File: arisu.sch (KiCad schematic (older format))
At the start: 40 parts, among them J1 USB_B_Micro, J10 PF6, J11 PF7, J12 VCC, J13 D+, J14 D-, J15 GND, J2 MISO, J3 VCC, J4 SCK, J5 MOSI, J6 RES, J7 GND, J8 PF4, J9 PF5, U1 USBLC6-2SC6, U2 ATmega32U4-AU, Y1 Crystal_GND24

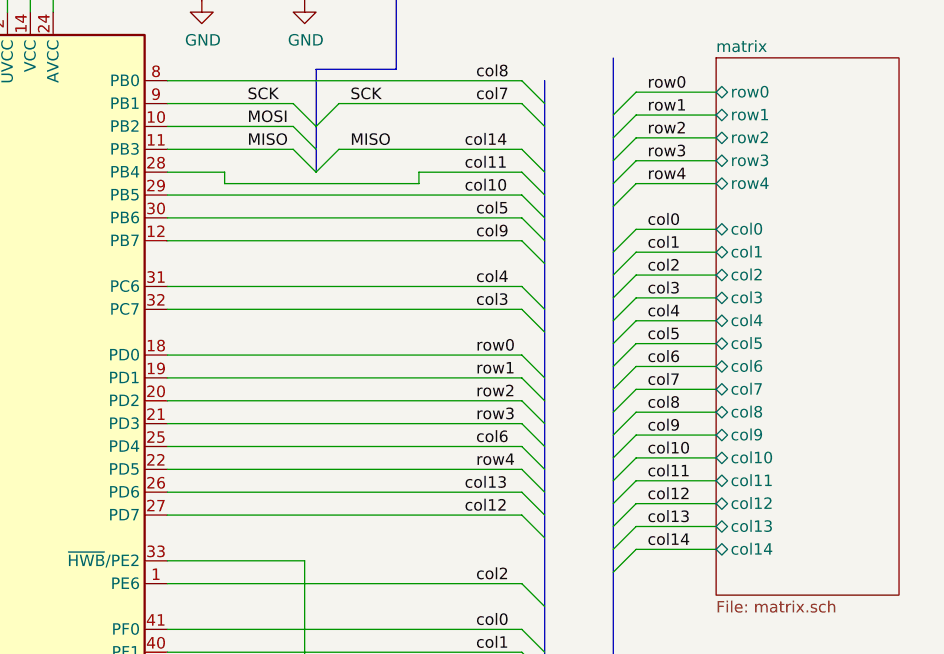
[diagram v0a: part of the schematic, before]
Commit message: Remove top row and decrease all other row indexes by 1 to adjust.
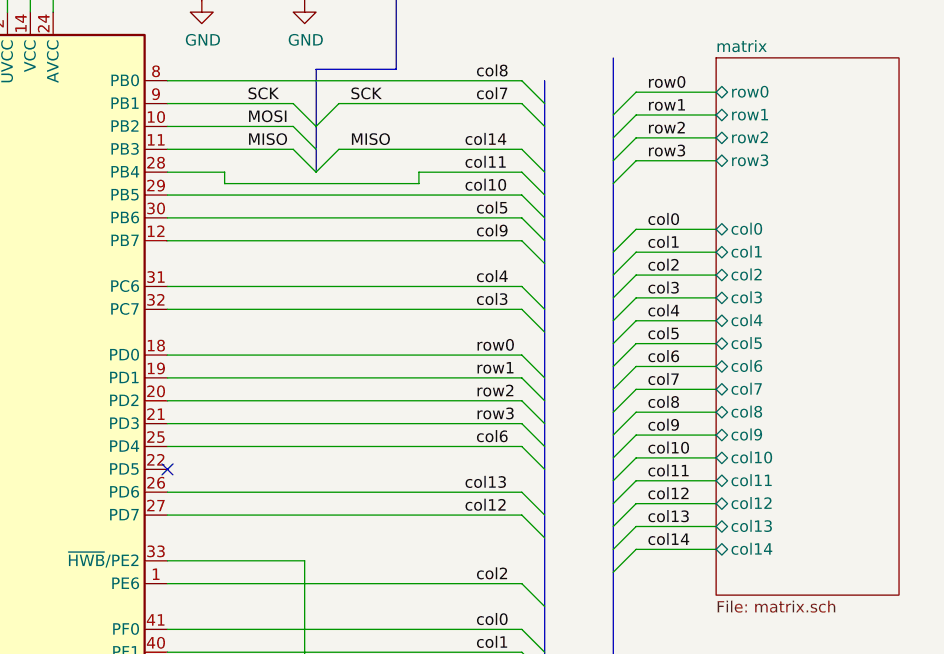
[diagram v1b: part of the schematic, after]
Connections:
- net row4: no longer names the net of U2.22 (PD5)
- no-connect marks 4 -> 5
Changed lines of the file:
@@
 EESchema Schematic File Version 4
 LIBS:arisu-cache
-EELAYER 26 0
+EELAYER 29 0
 EELAYER END
 $Descr A4 11693 8268
@@
 	5100 4350 6650 4350
 Wire Wire Line
-	5100 4450 6650 4450
-Wire Wire Line
 	5100 4550 6650 4550
 Wire Wire Line
@@
 Entry Wire Line
 	6650 4350 6750 4450
-Entry Wire Line
-	6650 4450 6750 4550
 Entry Wire Line
 	6650 4550 6750 4650
@@
 Text Label 6450 4250 0    50   ~ 0
 row3
-Text Label 6450 4450 0    50   ~ 0
-row4
 Text Label 6450 5150 0    50   ~ 0
 col0
@@
 F4 "row2" T L 7500 3000 50
 F5 "row3" T L 7500 3100 50
-F6 "row4" T L 7500 3200 50
-F7 "col0" T L 7500 3400 50
-F8 "col1" T L 7500 3500 50
-F9 "col2" T L 7500 3600 50
-F10 "col3" T L 7500 3700 50
-F11 "col4" T L 7500 3800 50
-F12 "col5" T L 7500 3900 50
-F13 "col6" T L 7500 4000 50
-F14 "col7" T L 7500 4100 50
-F15 "col8" T L 7500 4200 50
-F16 "col9" T L 7500 4300 50
-F17 "col10" T L 7500 4400 50
-F18 "col11" T L 7500 4500 50
-F19 "col12" T L 7500 4600 50
-F20 "col13" T L 7500 4700 50
-F21 "col14" T L 7500 4800 50
+F6 "col0" T L 7500 3400 50
+F7 "col1" T L 7500 3500 50
+F8 "col2" T L 7500 3600 50
+F9 "col3" T L 7500 3700 50
+F10 "col4" T L 7500 3800 50
+F11 "col5" T L 7500 3900 50
+F12 "col6" T L 7500 4000 50
+F13 "col7" T L 7500 4100 50
+F14 "col8" T L 7500 4200 50
+F15 "col9" T L 7500 4300 50
+F16 "col10" T L 7500 4400 50
+F17 "col11" T L 7500 4500 50
+F18 "col12" T L 7500 4600 50
+F19 "col13" T L 7500 4700 50
+F20 "col14" T L 7500 4800 50
 $EndSheet
 Wire Wire Line
@@
 Entry Wire Line
 	7050 3200 7150 3100
-Entry Wire Line
-	7050 3300 7150 3200
 Wire Wire Line
 	7150 3000 7500 3000
 Wire Wire Line
 	7150 3100 7500 3100
-Wire Wire Line
-	7150 3200 7500 3200
 Entry Wire Line
 	7050 3500 7150 3400
@@
 Wire Wire Line
 	5100 3150 5350 3150
-Text Label 7200 3200 0    50   ~ 0
-row4
 Text Label 7200 2800 0    50   ~ 0
 row0
@@
 	1    0    0    -1
 $EndComp
+$Comp
+L Mechanical:MountingHole H3
+U 1 1 5C59C18D
+P 8700 3100
+F 0 "H3" H 8800 3146 50  0000 L CNN
+F 1 "MountingHole" H 8800 3055 50  0000 L CNN
+F 2 "Mounting_Holes:MountingHole_2.2mm_M2_Pad" H 8700 3100 50  0001 C CNN
+F 3 "~" H 8700 3100 50  0001 C CNN
+	1    8700 3100
+	1    0    0    -1
+$EndComp
+$Comp
+L Mechanical:MountingHole H4
+U 1 1 5C59C1E9
+P 8700 3300
+F 0 "H4" H 8800 3346 50  0000 L CNN
+F 1 "MountingHole" H 8800 3255 50  0000 L CNN
+F 2 "Mounting_Holes:MountingHole_2.2mm_M2_Pad" H 8700 3300 50  0001 C CNN
+F 3 "~" H 8700 3300 50  0001 C CNN
+	1    8700 3300
+	1    0    0    -1
+$EndComp
+$Comp
+L Mechanical:MountingHole H5
+U 1 1 5C59C249
+P 8700 3500
+F 0 "H5" H 8800 3546 50  0000 L CNN
+F 1 "MountingHole" H 8800 3455 50  0000 L CNN
+F 2 "Mounting_Holes:MountingHole_2.2mm_M2_Pad" H 8700 3500 50  0001 C CNN
+F 3 "~" H 8700 3500 50  0001 C CNN
+	1    8700 3500
+	1    0    0    -1
+$EndComp
+$Comp
+L Mechanical:MountingHole H6
+U 1 1 5C59C2A7
+P 8700 3700
+F 0 "H6" H 8800 3746 50  0000 L CNN
+F 1 "MountingHole" H 8800 3655 50  0000 L CNN
+F 2 "Mounting_Holes:MountingHole_2.2mm_M2_Pad" H 8700 3700 50  0001 C CNN
+F 3 "~" H 8700 3700 50  0001 C CNN
+	1    8700 3700
+	1    0    0    -1
+$EndComp
+$Comp
+L Mechanical:MountingHole H7
+U 1 1 5C59C305
+P 8700 3900
+F 0 "H7" H 8800 3946 50  0000 L CNN
+F 1 "MountingHole" H 8800 3855 50  0000 L CNN
+F 2 "Mounting_Holes:MountingHole_2.2mm_M2_Pad" H 8700 3900 50  0001 C CNN
+F 3 "~" H 8700 3900 50  0001 C CNN
+	1    8700 3900
+	1    0    0    -1
+$EndComp
+$Comp
+L Mechanical:MountingHole H8
+U 1 1 5C59C367
+P 8700 4100
+F 0 "H8" H 8800 4146 50  0000 L CNN
+F 1 "MountingHole" H 8800 4055 50  0000 L CNN
+F 2 "Mounting_Holes:MountingHole_2.2mm_M2_Pad" H 8700 4100 50  0001 C CNN
+F 3 "~" H 8700 4100 50  0001 C CNN
+	1    8700 4100
+	1    0    0    -1
+$EndComp
+NoConn ~ 5100 4450
 Wire Bus Line
 	5750 2700 5750 3150
@@
 Wire Bus Line
 	7050 2650 7050 5800
-$Comp
-L Mechanical:MountingHole H3
-U 1 1 5C59C18D
-P 8700 3100
-F 0 "H3" H 8800 3146 50  0000 L CNN
-F 1 "MountingHole" H 8800 3055 50  0000 L CNN
-F 2 "Mounting_Holes:MountingHole_2.2mm_M2_Pad" H 8700 3100 50  0001 C CNN
-F 3 "~" H 8700 3100 50  0001 C CNN
-	1    8700 3100
-	1    0    0    -1
-$EndComp
-$Comp
-L Mechanical:MountingHole H4
-U 1 1 5C59C1E9
-P 8700 3300
-F 0 "H4" H 8800 3346 50  0000 L CNN
-F 1 "MountingHole" H 8800 3255 50  0000 L CNN
-F 2 "Mounting_Holes:MountingHole_2.2mm_M2_Pad" H 8700 3300 50  0001 C CNN
-F 3 "~" H 8700 3300 50  0001 C CNN
-	1    8700 3300
-	1    0    0    -1
-$EndComp
-$Comp
-L Mechanical:MountingHole H5
-U 1 1 5C59C249
-P 8700 3500
-F 0 "H5" H 8800 3546 50  0000 L CNN
-F 1 "MountingHole" H 8800 3455 50  0000 L CNN
-F 2 "Mounting_Holes:MountingHole_2.2mm_M2_Pad" H 8700 3500 50  0001 C CNN
-F 3 "~" H 8700 3500 50  0001 C CNN
-	1    8700 3500
-	1    0    0    -1
-$EndComp
-$Comp
-L Mechanical:MountingHole H6
-U 1 1 5C59C2A7
-P 8700 3700
-F 0 "H6" H 8800 3746 50  0000 L CNN
-F 1 "MountingHole" H 8800 3655 50  0000 L CNN
-F 2 "Mounting_Holes:MountingHole_2.2mm_M2_Pad" H 8700 3700 50  0001 C CNN
-F 3 "~" H 8700 3700 50  0001 C CNN
-	1    8700 3700
-	1    0    0    -1
-$EndComp
-$Comp
-L Mechanical:MountingHole H7
-U 1 1 5C59C305
-P 8700 3900
-F 0 "H7" H 8800 3946 50  0000 L CNN
-F 1 "MountingHole" H 8800 3855 50  0000 L CNN
-F 2 "Mounting_Holes:MountingHole_2.2mm_M2_Pad" H 8700 3900 50  0001 C CNN
-F 3 "~" H 8700 3900 50  0001 C CNN
-	1    8700 3900
-	1    0    0    -1
-$EndComp
-$Comp
-L Mechanical:MountingHole H8
-U 1 1 5C59C367
-P 8700 4100
-F 0 "H8" H 8800 4146 50  0000 L CNN
-F 1 "MountingHole" H 8800 4055 50  0000 L CNN
-F 2 "Mounting_Holes:MountingHole_2.2mm_M2_Pad" H 8700 4100 50  0001 C CNN
-F 3 "~" H 8700 4100 50  0001 C CNN
-	1    8700 4100
-	1    0    0    -1
-$EndComp
 $EndSCHEMATC

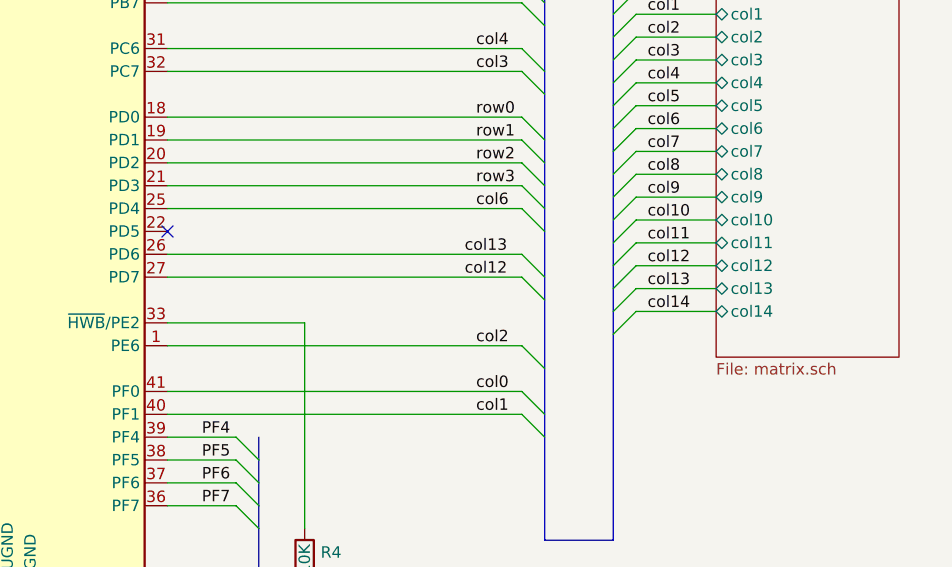
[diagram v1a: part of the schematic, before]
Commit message: Redesign alpha layout for natural finger spread.
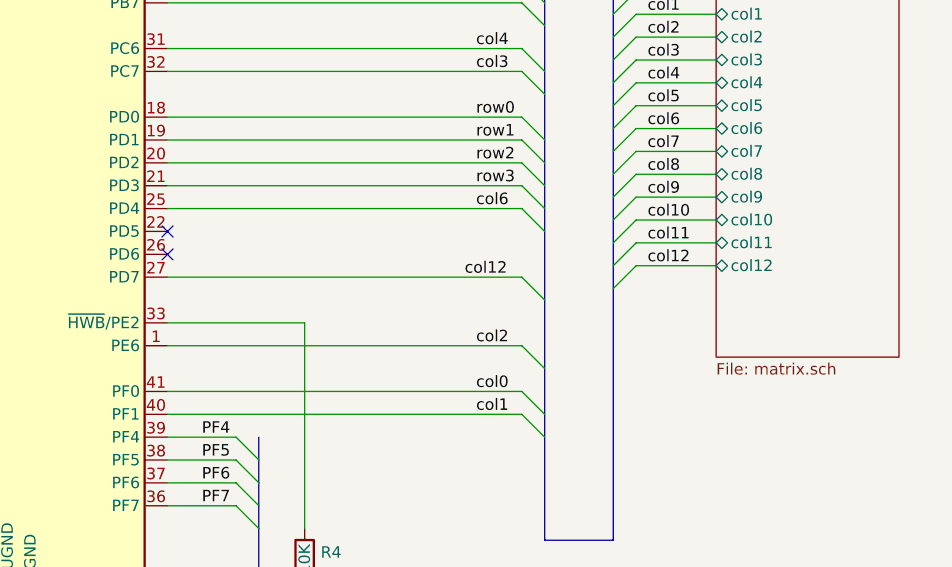
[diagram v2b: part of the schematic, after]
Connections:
- net col13: no longer names the net of U2.26 (PD6)
- no-connect marks 5 -> 6
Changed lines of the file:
@@
 	5100 4350 6650 4350
 Wire Wire Line
-	5100 4550 6650 4550
-Wire Wire Line
 	5100 4650 6650 4650
 Entry Wire Line
@@
 Entry Wire Line
 	6650 4350 6750 4450
-Entry Wire Line
-	6650 4550 6750 4650
 Entry Wire Line
 	6650 4650 6750 4750
@@
 Text Label 6400 4650 0    50   ~ 0
 col12
-Text Label 6400 4550 0    50   ~ 0
-col13
 Text Label 6400 3050 0    50   ~ 0
 col14
@@
 F17 "col11" T L 7500 4500 50
 F18 "col12" T L 7500 4600 50
-F19 "col13" T L 7500 4700 50
-F20 "col14" T L 7500 4800 50
 $EndSheet
 Wire Wire Line
@@
 Entry Wire Line
 	7050 4700 7150 4600
-Entry Wire Line
-	7050 4800 7150 4700
-Entry Wire Line
-	7050 4900 7150 4800
-Wire Wire Line
-	7150 4800 7500 4800
-Wire Wire Line
-	7150 4700 7500 4700
 Wire Wire Line
 	7150 4600 7500 4600
@@
 Text Label 7200 3500 0    50   ~ 0
 col1
-Text Label 7200 4800 0    50   ~ 0
-col14
-Text Label 7200 4700 0    50   ~ 0
-col13
 Text Label 7200 4600 0    50   ~ 0
 col12
@@
 $EndComp
 NoConn ~ 5100 4450
+NoConn ~ 5100 4550
 Wire Bus Line
 	5750 2700 5750 3150

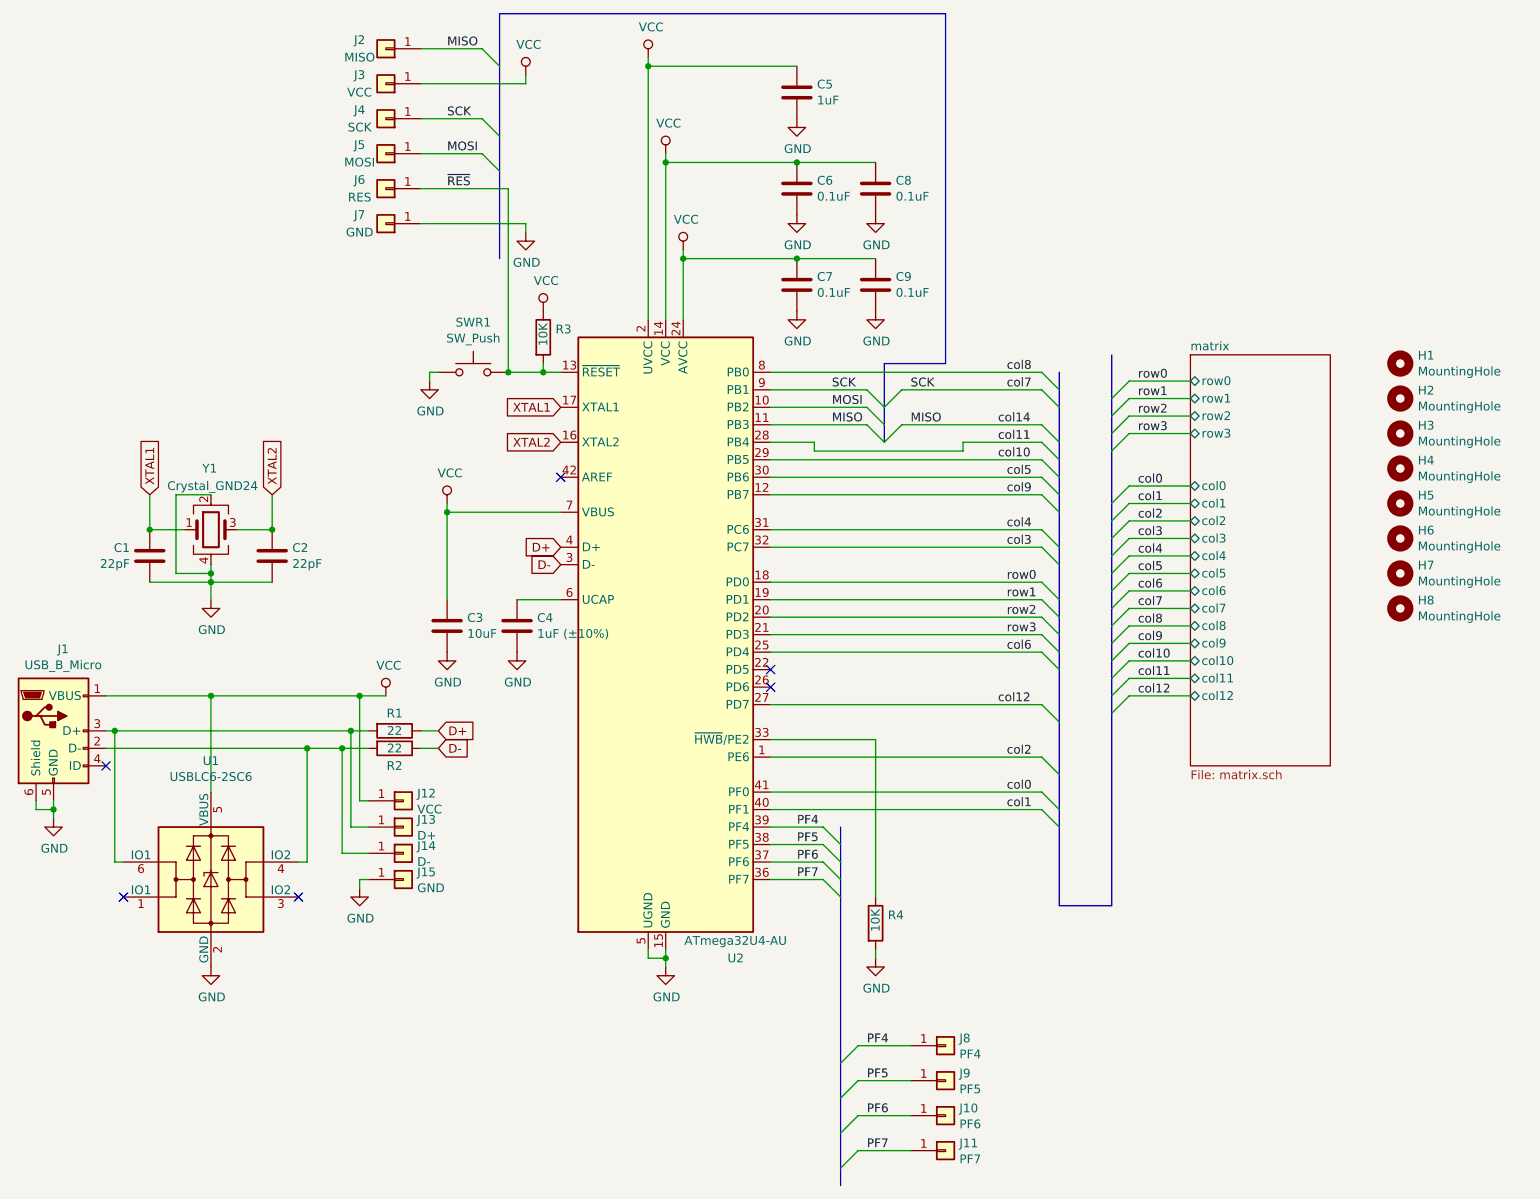
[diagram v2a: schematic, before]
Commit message: Finish ergo layout and route some rows.
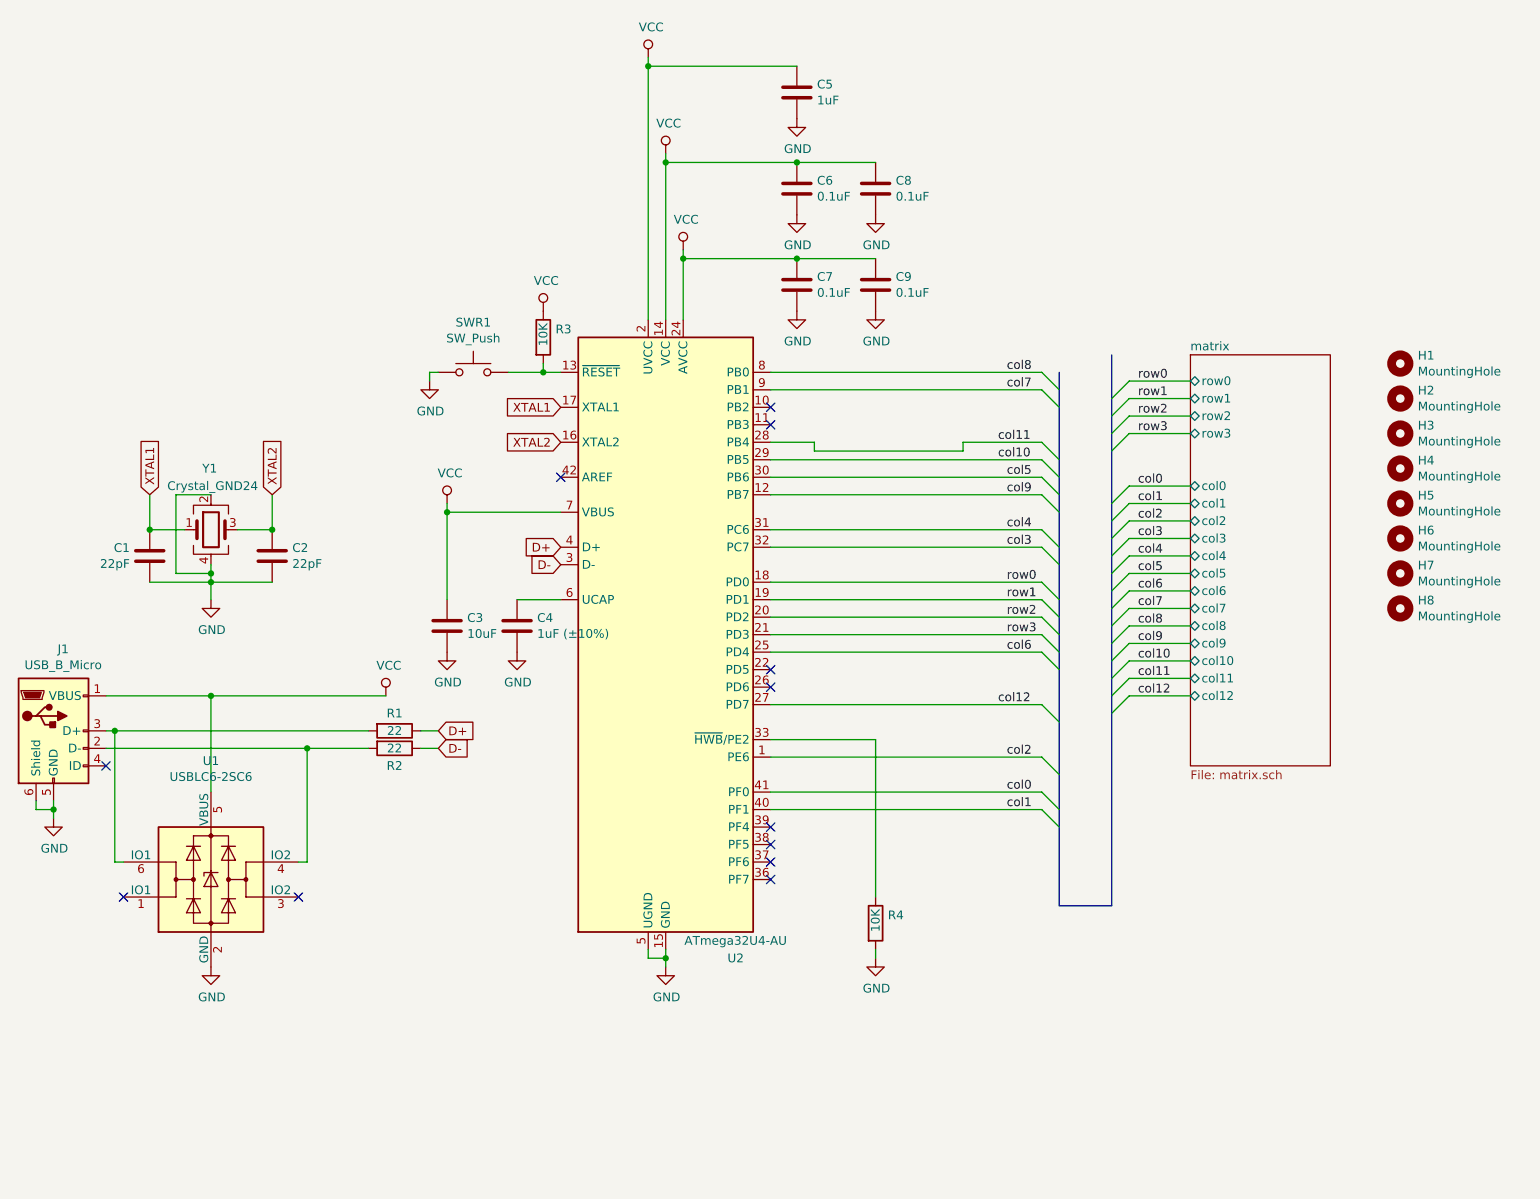
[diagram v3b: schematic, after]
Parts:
- removed J10: PF6, Pin_Headers:Pin_Header_Straight_1x01_Pitch2.54mm, symbol Connector_Generic:Conn_01x01
- removed J11: PF7, Pin_Headers:Pin_Header_Straight_1x01_Pitch2.54mm, symbol Connector_Generic:Conn_01x01
- removed J12, J3: VCC, Pin_Headers:Pin_Header_Straight_1x01_Pitch2.54mm, symbol Connector_Generic:Conn_01x01
- removed J13: D+, Pin_Headers:Pin_Header_Straight_1x01_Pitch2.54mm, symbol Connector_Generic:Conn_01x01
- removed J14: D-, Pin_Headers:Pin_Header_Straight_1x01_Pitch2.54mm, symbol Connector_Generic:Conn_01x01
- removed J15, J7: GND, Pin_Headers:Pin_Header_Straight_1x01_Pitch2.54mm, symbol Connector_Generic:Conn_01x01
- removed J2: MISO, Pin_Headers:Pin_Header_Straight_1x01_Pitch2.54mm, symbol Connector_Generic:Conn_01x01
- removed J4: SCK, Pin_Headers:Pin_Header_Straight_1x01_Pitch2.54mm, symbol Connector_Generic:Conn_01x01
- removed J5: MOSI, Pin_Headers:Pin_Header_Straight_1x01_Pitch2.54mm, symbol Connector_Generic:Conn_01x01
- removed J6: RES, Pin_Headers:Pin_Header_Straight_1x01_Pitch2.54mm, symbol Connector_Generic:Conn_01x01
- removed J8: PF4, Pin_Headers:Pin_Header_Straight_1x01_Pitch2.54mm, symbol Connector_Generic:Conn_01x01
- removed J9: PF5, Pin_Headers:Pin_Header_Straight_1x01_Pitch2.54mm, symbol Connector_Generic:Conn_01x01
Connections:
- net MISO: no longer names the net of U2.11 (PB3)
- net MOSI: no longer names the net of U2.10 (PB2)
- net PF4: no longer names the net of U2.39 (PF4)
- net PF5: no longer names the net of U2.38 (PF5)
- net PF6: no longer names the net of U2.37 (PF6)
- net PF7: no longer names the net of U2.36 (PF7)
- net SCK renamed col7
- net ~RES~: no longer names the net of R3.2, SWR1.2, U2.13 (~RESET)
- no-connect marks 6 -> 12
